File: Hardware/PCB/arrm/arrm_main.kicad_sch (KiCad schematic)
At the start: 47 parts, among them J10 AudioJack2, J11 Synth_power_2x5, J7 AudioJack2, J8 AudioJack2, J9 AudioJack2, U1 NE5532, U2 TL072

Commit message: Rename project, cleanup
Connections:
- net CARRLVL_CW renamed CARRLVL_WIP
- net SIGLVL_CW renamed SIGLVL_WIP
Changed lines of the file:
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@@
     (effects (font (size 1.27 1.27)) (justify left bottom))
   )
-  (hierarchical_label "CARRLVL_CW" (shape output) (at 105.41 90.17 90)
+  (hierarchical_label "CARRLVL_WIP" (shape output) (at 105.41 90.17 90)
     (effects (font (size 1.27 1.27)) (justify left))
   )
@@
     (effects (font (size 1.27 1.27)) (justify right))
   )
-  (hierarchical_label "SIGLVL_CW" (shape output) (at 138.43 36.83 90)
+  (hierarchical_label "SIGLVL_WIP" (shape output) (at 138.43 36.83 90)
     (effects (font (size 1.27 1.27)) (justify left))
   )

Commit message: Final pre fab tweaks, Gerbers
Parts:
- C1: renamed from C3; value 10uF -> (none); footprint ao_tht:C_Radial_D8.0mm_H11.5mm_P3.50mm -> (none); SKU (none) -> A-4216
- C10: renamed from C5; value 47pF -> (none); footprint ao_tht:C_Disc_D5.0mm_W2.5mm_P5.00mm -> (none)
- C11: renamed from C2; value 47pF -> (none); footprint ao_tht:C_Disc_D5.0mm_W2.5mm_P5.00mm -> (none)
- C2: renamed from C4; value 47pF -> (none); footprint ao_tht:C_Disc_D5.0mm_W2.5mm_P5.00mm -> (none)
- C3: renamed from C6; value 10uF -> (none); footprint ao_tht:CP_Radial_D6.3mm_P2.50mm -> (none)
- C4: renamed from C9; value 10uF -> (none); footprint ao_tht:CP_Radial_D6.3mm_P2.50mm -> (none)
- C5: renamed from C7; value 100nF -> (none); footprint ao_tht:C_Disc_D3.0mm_W1.6mm_P2.50mm -> (none)
- C6: renamed from C10; value 100nF -> (none); footprint ao_tht:C_Disc_D3.0mm_W1.6mm_P2.50mm -> (none)
- C7: renamed from C1; value 47pF -> (none); footprint ao_tht:C_Disc_D5.0mm_W2.5mm_P5.00mm -> (none)
- C8: value 100nF -> (none); footprint ao_tht:C_Disc_D3.0mm_W1.6mm_P2.50mm -> (none)
- C9: renamed from C11; value 100nF -> (none); footprint ao_tht:C_Disc_D3.0mm_W1.6mm_P2.50mm -> (none)
- D1: renamed from D5; value 1N5817 -> (none); footprint ao_tht:D_DO-41_SOD81_P10.16mm_Horizontal -> (none)
- D2: renamed from D6; value 1N5817 -> (none); footprint ao_tht:D_DO-41_SOD81_P10.16mm_Horizontal -> (none)
- D3: renamed from D2; value 1N695 -> (none); footprint ringmod:D_DO-7_P10.16mm_Horizontal -> (none)
- D4: renamed from D1; value 1N695 -> (none); footprint ringmod:D_DO-7_P10.16mm_Horizontal -> (none)
- D5: renamed from D4; value 1N695 -> (none); footprint ringmod:D_DO-7_P10.16mm_Horizontal -> (none)
- D6: renamed from D3; value 1N695 -> (none); footprint ringmod:D_DO-7_P10.16mm_Horizontal -> (none)
- GRAF1: value Holes -> (none); footprint ringmod:ringmod_panel_2_holes -> (none)
- J10: renamed from J9; value AudioJack2 -> (none); footprint ao_tht:Jack_6.35mm_PJ_629HAN_slots -> (none)
- J11: renamed from J10; value AudioJack2 -> (none); footprint ao_tht:Jack_6.35mm_PJ_629HAN_slots -> (none)
- J7: renamed from J11; value Synth_power_2x5 -> (none); footprint ao_tht:Power_Header -> (none)
- J8: renamed from J7; value AudioJack2 -> (none); footprint ao_tht:Jack_6.35mm_PJ_629HAN_slots -> (none)
- J9: renamed from J8; value AudioJack2 -> (none); footprint ao_tht:Jack_6.35mm_PJ_629HAN_slots -> (none)
- R1: renamed from R8; value 1M -> (none); footprint ao_tht:R_Axial_DIN0207_L6.3mm_D2.5mm_P10.16mm_Horizontal -> (none)
- R10: renamed from R6; value 100k -> (none); footprint ao_tht:R_Axial_DIN0207_L6.3mm_D2.5mm_P10.16mm_Horizontal -> (none)
- R11: renamed from R12; value 10k -> (none); footprint ao_tht:R_Axial_DIN0207_L6.3mm_D2.5mm_P10.16mm_Horizontal -> (none)
- R12: renamed from R5; value 100k -> (none); footprint ao_tht:R_Axial_DIN0207_L6.3mm_D2.5mm_P10.16mm_Horizontal -> (none)
- R13: value 1k -> (none); footprint ao_tht:R_Axial_DIN0207_L6.3mm_D2.5mm_P10.16mm_Horizontal -> (none)
- R14: value 100k -> (none); footprint ao_tht:R_Axial_DIN0207_L6.3mm_D2.5mm_P10.16mm_Horizontal -> (none)
- R2: renamed from R4; value 100k -> (none); footprint ao_tht:R_Axial_DIN0207_L6.3mm_D2.5mm_P10.16mm_Horizontal -> (none)
- R3: renamed from R7; value 100k -> (none); footprint ao_tht:R_Axial_DIN0207_L6.3mm_D2.5mm_P10.16mm_Horizontal -> (none)
- R4: renamed from R9; value 330R -> (none); footprint ao_tht:R_Axial_DIN0207_L6.3mm_D2.5mm_P10.16mm_Horizontal -> (none)
- R5: renamed from R10; value 330R -> (none); footprint ao_tht:R_Axial_DIN0207_L6.3mm_D2.5mm_P10.16mm_Horizontal -> (none)
- R6: renamed from R1; value 100k -> (none); footprint ao_tht:R_Axial_DIN0207_L6.3mm_D2.5mm_P10.16mm_Horizontal -> (none)
- R7: renamed from R2; value 330R -> (none); footprint ao_tht:R_Axial_DIN0207_L6.3mm_D2.5mm_P10.16mm_Horizontal -> (none)
- R8: renamed from R11; value 100k -> (none); footprint ao_tht:R_Axial_DIN0207_L6.3mm_D2.5mm_P10.16mm_Horizontal -> (none)
- R9: renamed from R3; value 100k -> (none); footprint ao_tht:R_Axial_DIN0207_L6.3mm_D2.5mm_P10.16mm_Horizontal -> (none)
- RV4: renamed from RV7; value 20k -> (none); footprint ao_tht:Potentiometer_Bourns_3296W_Vertical_standard -> (none)
- RV5: renamed from RV8; value 20k -> (none); footprint ao_tht:Potentiometer_Bourns_3296W_Vertical_standard -> (none)
- RV6: renamed from RV9; value 100k -> (none); footprint ao_tht:Potentiometer_Bourns_3296W_Vertical_standard -> (none)
- TP1: value -12V -> (none); footprint ao_tht:TestPoint_THTPad_D1.5mm_Drill0.7mm -> (none)
- TP2: value +12V -> (none); footprint ao_tht:TestPoint_THTPad_D1.5mm_Drill0.7mm -> (none)
- TP3: value GND -> (none); footprint ao_tht:TestPoint_THTPad_1.5x1.5mm_Drill0.7mm -> (none)
- TR1, TR2: value TY-141P -> (none); footprint ringmod:Transformer_TY-141P -> (none)
- U1: value NE5532 -> (none); footprint ao_tht:DIP-8_W7.62mm_Socket_LongPads -> (none)
- U2: value TL072 -> (none); footprint ao_tht:DIP-8_W7.62mm_Socket_LongPads -> (none)

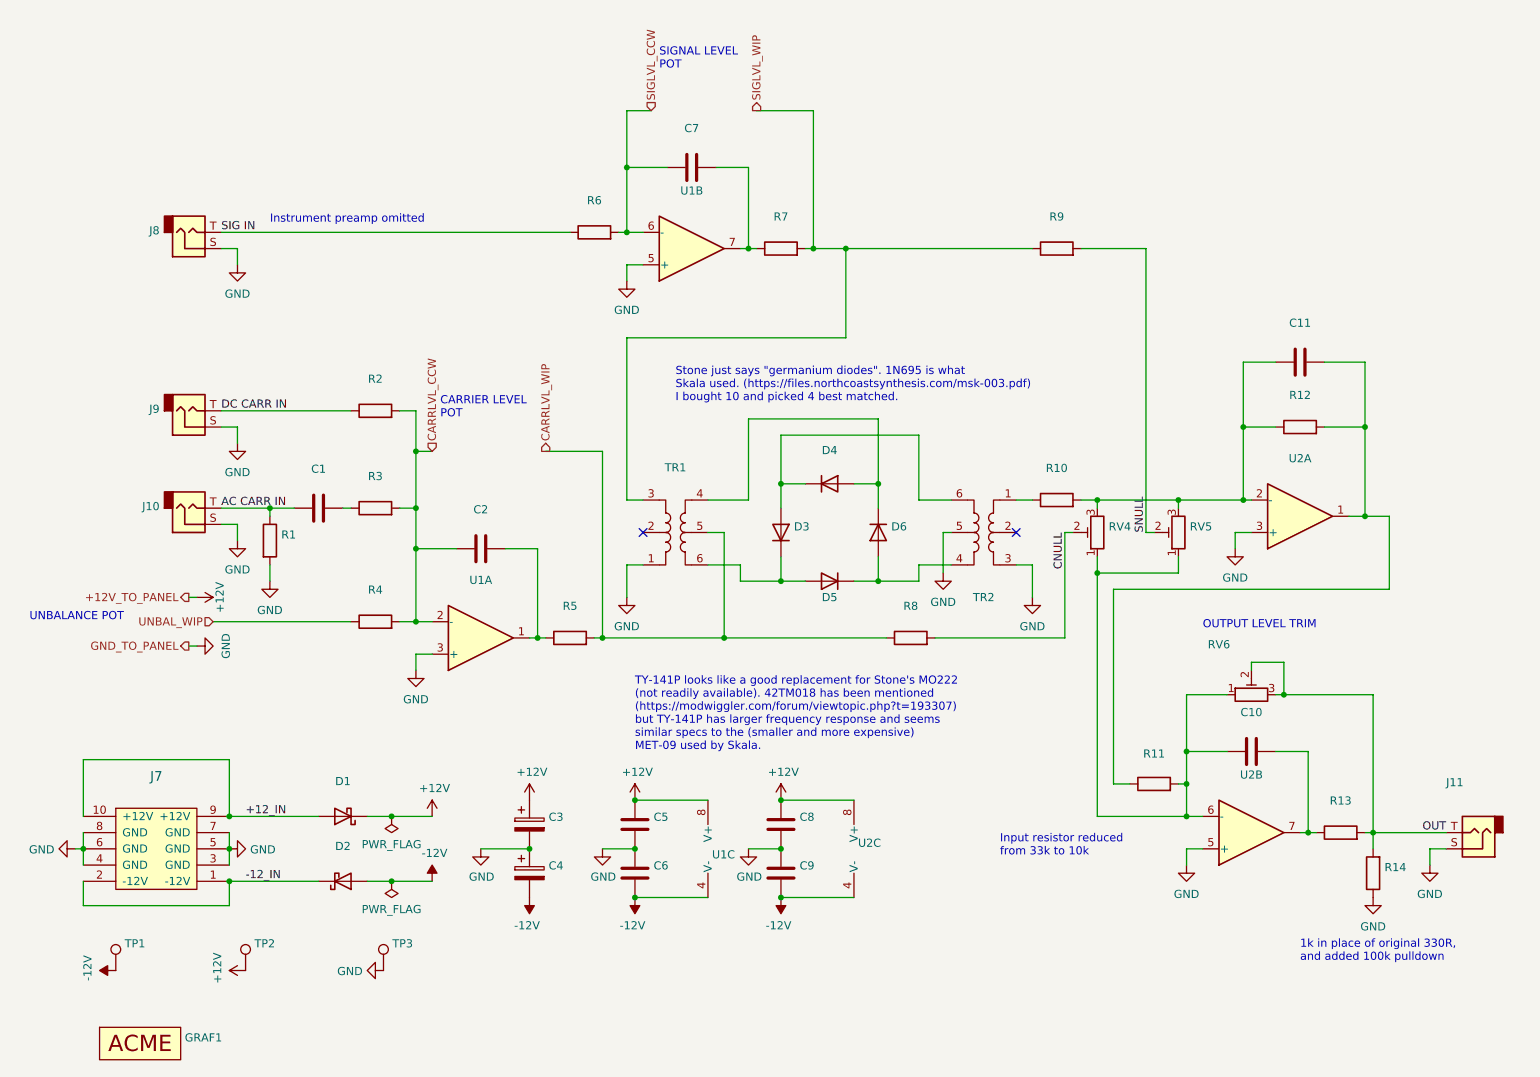
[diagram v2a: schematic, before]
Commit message: Fix footprint path; fix transformer footprint
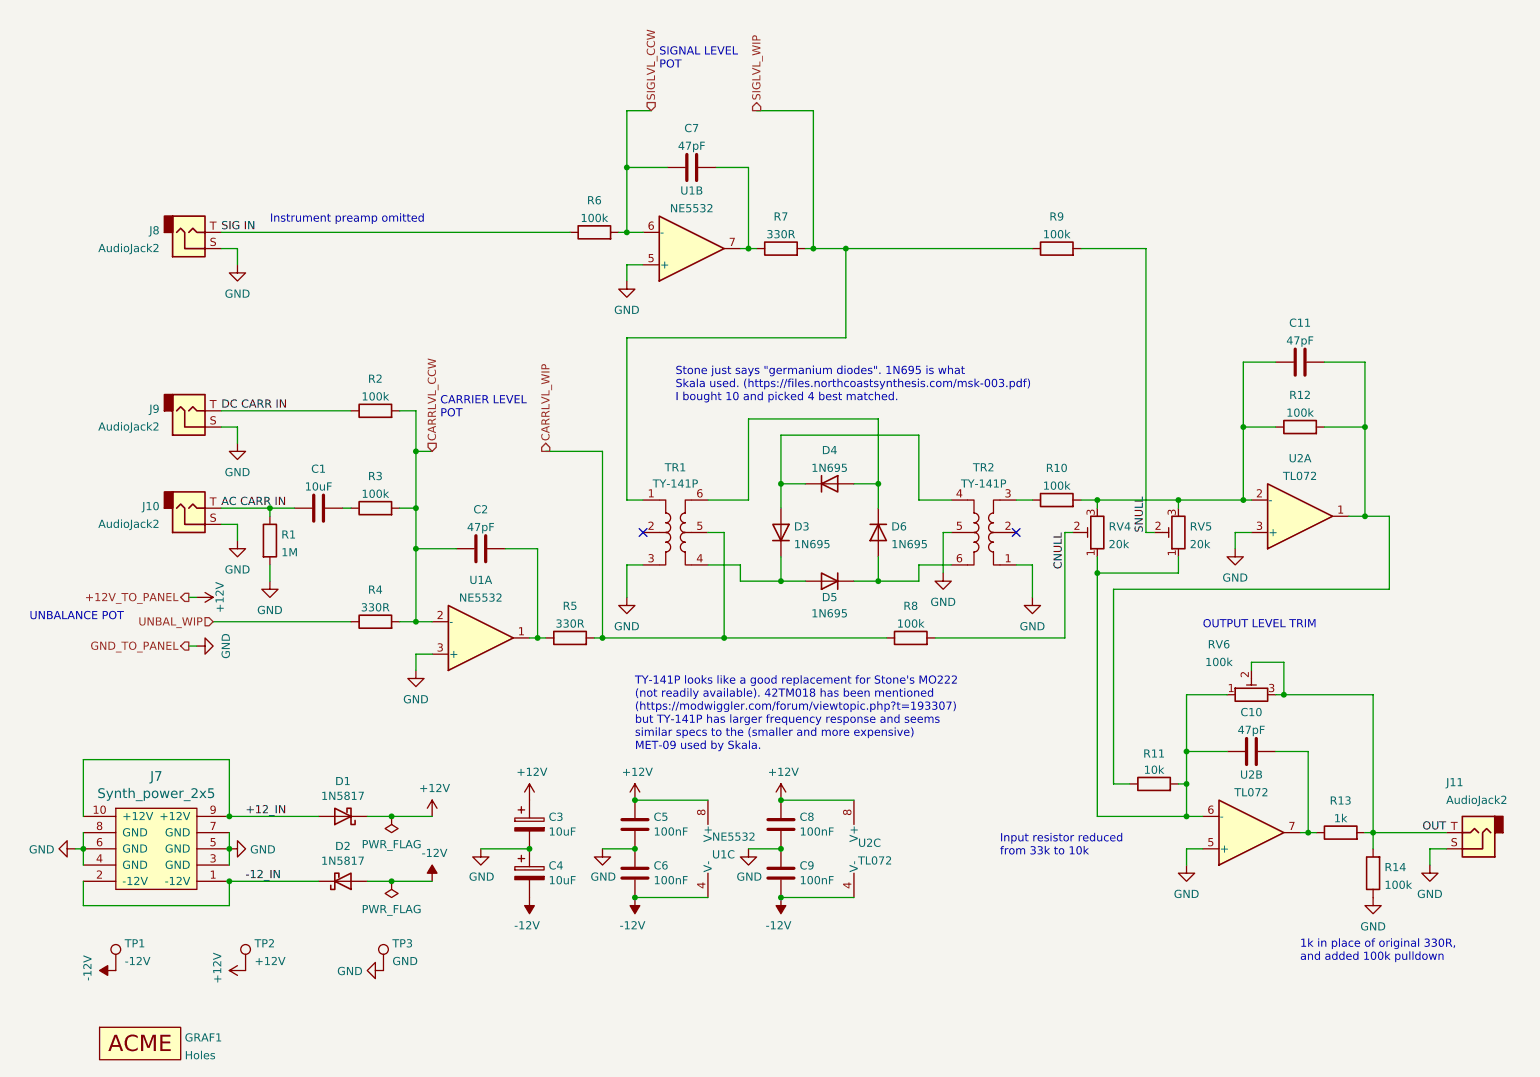
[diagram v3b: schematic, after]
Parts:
- C1: value (none) -> 10uF; footprint (none) -> ao_tht:C_Radial_D8.0mm_H11.5mm_P3.50mm
- C10, C11, C2, C7: value (none) -> 47pF; footprint (none) -> ao_tht:C_Disc_D5.0mm_W2.5mm_P5.00mm
- C3, C4: value (none) -> 10uF; footprint (none) -> ao_tht:CP_Radial_D6.3mm_P2.50mm
- C5, C6, C8, C9: value (none) -> 100nF; footprint (none) -> ao_tht:C_Disc_D3.0mm_W1.6mm_P2.50mm
- D1, D2: value (none) -> 1N5817; footprint (none) -> ao_tht:D_DO-41_SOD81_P10.16mm_Horizontal
- D3, D4, D5, D6: value (none) -> 1N695; footprint (none) -> ringmod:D_DO-7_P10.16mm_Horizontal
- GRAF1: value (none) -> Holes; footprint (none) -> ringmod:ringmod_panel_2_holes
- J10, J11, J8, J9: value (none) -> AudioJack2; footprint (none) -> ao_tht:Jack_6.35mm_PJ_629HAN_slots
- J7: value (none) -> Synth_power_2x5; footprint (none) -> ao_tht:Power_Header
- R1: value (none) -> 1M; footprint (none) -> ao_tht:R_Axial_DIN0207_L6.3mm_D2.5mm_P10.16mm_Horizontal
- R10, R12, R14, R2, R3, R6, R8, R9: value (none) -> 100k; footprint (none) -> ao_tht:R_Axial_DIN0207_L6.3mm_D2.5mm_P10.16mm_Horizontal
- R11: value (none) -> 10k; footprint (none) -> ao_tht:R_Axial_DIN0207_L6.3mm_D2.5mm_P10.16mm_Horizontal
- R13: value (none) -> 1k; footprint (none) -> ao_tht:R_Axial_DIN0207_L6.3mm_D2.5mm_P10.16mm_Horizontal
- R4, R5, R7: value (none) -> 330R; footprint (none) -> ao_tht:R_Axial_DIN0207_L6.3mm_D2.5mm_P10.16mm_Horizontal
- RV4, RV5: value (none) -> 20k; footprint (none) -> ao_tht:Potentiometer_Bourns_3296W_Vertical_standard
- RV6: value (none) -> 100k; footprint (none) -> ao_tht:Potentiometer_Bourns_3296W_Vertical_standard
- TP1: value (none) -> -12V; footprint (none) -> ao_tht:TestPoint_THTPad_D1.5mm_Drill0.7mm
- TP2: value (none) -> +12V; footprint (none) -> ao_tht:TestPoint_THTPad_D1.5mm_Drill0.7mm
- TP3: value (none) -> GND; footprint (none) -> ao_tht:TestPoint_THTPad_1.5x1.5mm_Drill0.7mm
- TR1, TR2: value (none) -> TY-141P; footprint (none) -> ringmod:Transformer_TY-141P
- U1: value (none) -> NE5532; footprint (none) -> ao_tht:DIP-8_W7.62mm_Socket_LongPads
- U2: value (none) -> TL072; footprint (none) -> ao_tht:DIP-8_W7.62mm_Socket_LongPads
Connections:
- net GND: now also TR1.3, TR2.1; no longer TR1.1, TR2.3
- net SIGLVL_WIP: now also TR1.1; no longer TR1.3
- net at D3.2 (A), D4.1 (K): now also TR2.4; no longer TR2.6
- net at D4.2 (A), D6.1 (K): now also TR1.6; no longer TR1.4
- net at D3.1 (K), D5.2 (A): now also TR1.4; no longer TR1.6
- net at R10.1: now also TR2.3; no longer TR2.1
- net at D5.1 (K), D6.2 (A): now also TR2.6; no longer TR2.4
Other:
- moved on the sheet: TR2

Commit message: Post fab updates
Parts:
- C1: value 10uF -> (none); footprint ao_tht:C_Radial_D8.0mm_H11.5mm_P3.50mm -> (none)
- C10, C11, C2, C7: value 47pF -> (none); footprint ao_tht:C_Disc_D5.0mm_W2.5mm_P5.00mm -> (none)
- C3, C4: value 10uF -> (none); footprint ao_tht:CP_Radial_D6.3mm_P2.50mm -> (none)
- C5, C6, C8, C9: value 100nF -> (none); footprint ao_tht:C_Disc_D3.0mm_W1.6mm_P2.50mm -> (none)
- D1, D2: value 1N5817 -> (none); footprint ao_tht:D_DO-41_SOD81_P10.16mm_Horizontal -> (none)
- D3, D4, D5, D6: value 1N695 -> (none); footprint ringmod:D_DO-7_P10.16mm_Horizontal -> (none)
- GRAF1: value Holes -> (none); footprint ringmod:ringmod_panel_2_holes -> (none)
- J10, J11, J8, J9: value AudioJack2 -> (none); footprint ao_tht:Jack_6.35mm_PJ_629HAN_slots -> (none)
- J7: value Synth_power_2x5 -> (none); footprint ao_tht:Power_Header -> (none)
- R1: value 1M -> (none); footprint ao_tht:R_Axial_DIN0207_L6.3mm_D2.5mm_P10.16mm_Horizontal -> (none)
- R10, R12, R14, R2, R3, R6, R8, R9: value 100k -> (none); footprint ao_tht:R_Axial_DIN0207_L6.3mm_D2.5mm_P10.16mm_Horizontal -> (none)
- R11: value 10k -> (none); footprint ao_tht:R_Axial_DIN0207_L6.3mm_D2.5mm_P10.16mm_Horizontal -> (none)
- R13: value 1k -> (none); footprint ao_tht:R_Axial_DIN0207_L6.3mm_D2.5mm_P10.16mm_Horizontal -> (none)
- R4, R5, R7: value 330R -> (none); footprint ao_tht:R_Axial_DIN0207_L6.3mm_D2.5mm_P10.16mm_Horizontal -> (none)
- RV4, RV5: value 20k -> (none); footprint ao_tht:Potentiometer_Bourns_3296W_Vertical_standard -> (none)
- RV6: value 100k -> (none); footprint ao_tht:Potentiometer_Bourns_3296W_Vertical_standard -> (none)
- TP1: value -12V -> (none); footprint ao_tht:TestPoint_THTPad_D1.5mm_Drill0.7mm -> (none)
- TP2: value +12V -> (none); footprint ao_tht:TestPoint_THTPad_D1.5mm_Drill0.7mm -> (none)
- TP3: value GND -> (none); footprint ao_tht:TestPoint_THTPad_1.5x1.5mm_Drill0.7mm -> (none)
- TR1, TR2: value TY-141P -> (none); footprint ringmod:Transformer_TY-141P -> (none)
- U1: value NE5532 -> (none); footprint ao_tht:DIP-8_W7.62mm_Socket_LongPads -> (none)
- U2: value TL072 -> (none); footprint ao_tht:DIP-8_W7.62mm_Socket_LongPads -> (none)

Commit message: Docs, pics, new Gerbers
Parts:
- J10, J11, J8, J9: SKU (none) -> A-1121; Vendor (none) -> Tayda
- RV4, RV5: SKU (none) -> A-592
- RV6: SKU (none) -> A-587
- U1: SKU (none) -> A-031; Vendor (none) -> Tayda
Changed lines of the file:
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@@
+      (effects (font (size 1.27 1.27)) hide)
+    )
+    (property "SKU" "A-1121" (id 5) (at 251.46 149.86 0)
+      (effects (font (size 1.27 1.27)) hide)
+    )
+    (property "Vendor" "Tayda" (id 6) (at 251.46 149.86 0)
       (effects (font (size 1.27 1.27)) hide)
     )
@@
     )
     (property "Datasheet" "http://www.ti.com/lit/ds/symlink/ne5532.pdf" (id 3) (at 95.25 119.38 0)
+      (effects (font (size 1.27 1.27)) hide)
+    )
+    (property "SKU" "A-031" (id 4) (at 95.25 119.38 0)
+      (effects (font (size 1.27 1.27)) hide)
+    )
+    (property "Vendor" "Tayda" (id 5) (at 95.25 119.38 0)
       (effects (font (size 1.27 1.27)) hide)
     )
@@
       (effects (font (size 1.27 1.27)) hide)
     )
+    (property "SKU" "A-587" (id 5) (at 215.9 128.27 0)
+      (effects (font (size 1.27 1.27)) hide)
+    )
     (pin "1")
     (pin "2")
@@
     )
     (property "Datasheet" "http://www.ti.com/lit/ds/symlink/ne5532.pdf" (id 3) (at 128.27 152.4 0)
+      (effects (font (size 1.27 1.27)) hide)
+    )
+    (property "SKU" "A-031" (id 4) (at 128.27 152.4 0)
+      (effects (font (size 1.27 1.27)) hide)
+    )
+    (property "Vendor" "Tayda" (id 5) (at 128.27 152.4 0)
       (effects (font (size 1.27 1.27)) hide)
     )
@@
       (effects (font (size 1.27 1.27)) hide)
     )
+    (property "SKU" "A-1121" (id 5) (at 49.53 99.06 0)
+      (effects (font (size 1.27 1.27)) hide)
+    )
+    (property "Vendor" "Tayda" (id 6) (at 49.53 99.06 0)
+      (effects (font (size 1.27 1.27)) hide)
+    )
     (pin "S")
     (pin "T")
@@
       (effects (font (size 1.27 1.27)) hide)
     )
+    (property "SKU" "A-1121" (id 5) (at 49.53 55.88 0)
+      (effects (font (size 1.27 1.27)) hide)
+    )
+    (property "Vendor" "Tayda" (id 6) (at 49.53 55.88 0)
+      (effects (font (size 1.27 1.27)) hide)
+    )
     (pin "S")
     (pin "T")
@@
     )
     (property "Vendor" "Tayda" (id 4) (at 191.77 102.87 0)
+      (effects (font (size 1.27 1.27)) hide)
+    )
+    (property "SKU" "A-592" (id 5) (at 191.77 102.87 0)
       (effects (font (size 1.27 1.27)) hide)
     )
@@
       (effects (font (size 1.27 1.27)) hide)
     )
+    (property "SKU" "A-592" (id 5) (at 204.47 102.87 0)
+      (effects (font (size 1.27 1.27)) hide)
+    )
     (pin "1")
     (pin "2")
@@
     )
     (property "Datasheet" "http://www.ti.com/lit/ds/symlink/ne5532.pdf" (id 3) (at 128.27 58.42 0)
+      (effects (font (size 1.27 1.27)) hide)
+    )
+    (property "SKU" "A-031" (id 4) (at 128.27 58.42 0)
+      (effects (font (size 1.27 1.27)) hide)
+    )
+    (property "Vendor" "Tayda" (id 5) (at 128.27 58.42 0)
       (effects (font (size 1.27 1.27)) hide)
     )
@@
       (effects (font (size 1.27 1.27)) hide)
     )
+    (property "SKU" "A-1121" (id 5) (at 49.53 83.82 0)
+      (effects (font (size 1.27 1.27)) hide)
+    )
+    (property "Vendor" "Tayda" (id 6) (at 49.53 83.82 0)
+      (effects (font (size 1.27 1.27)) hide)
+    )
